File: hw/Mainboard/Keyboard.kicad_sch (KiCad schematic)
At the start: 7 parts, among them J18 KEYBOARD, J19 KEYBOARD_EX, U19 74LS145

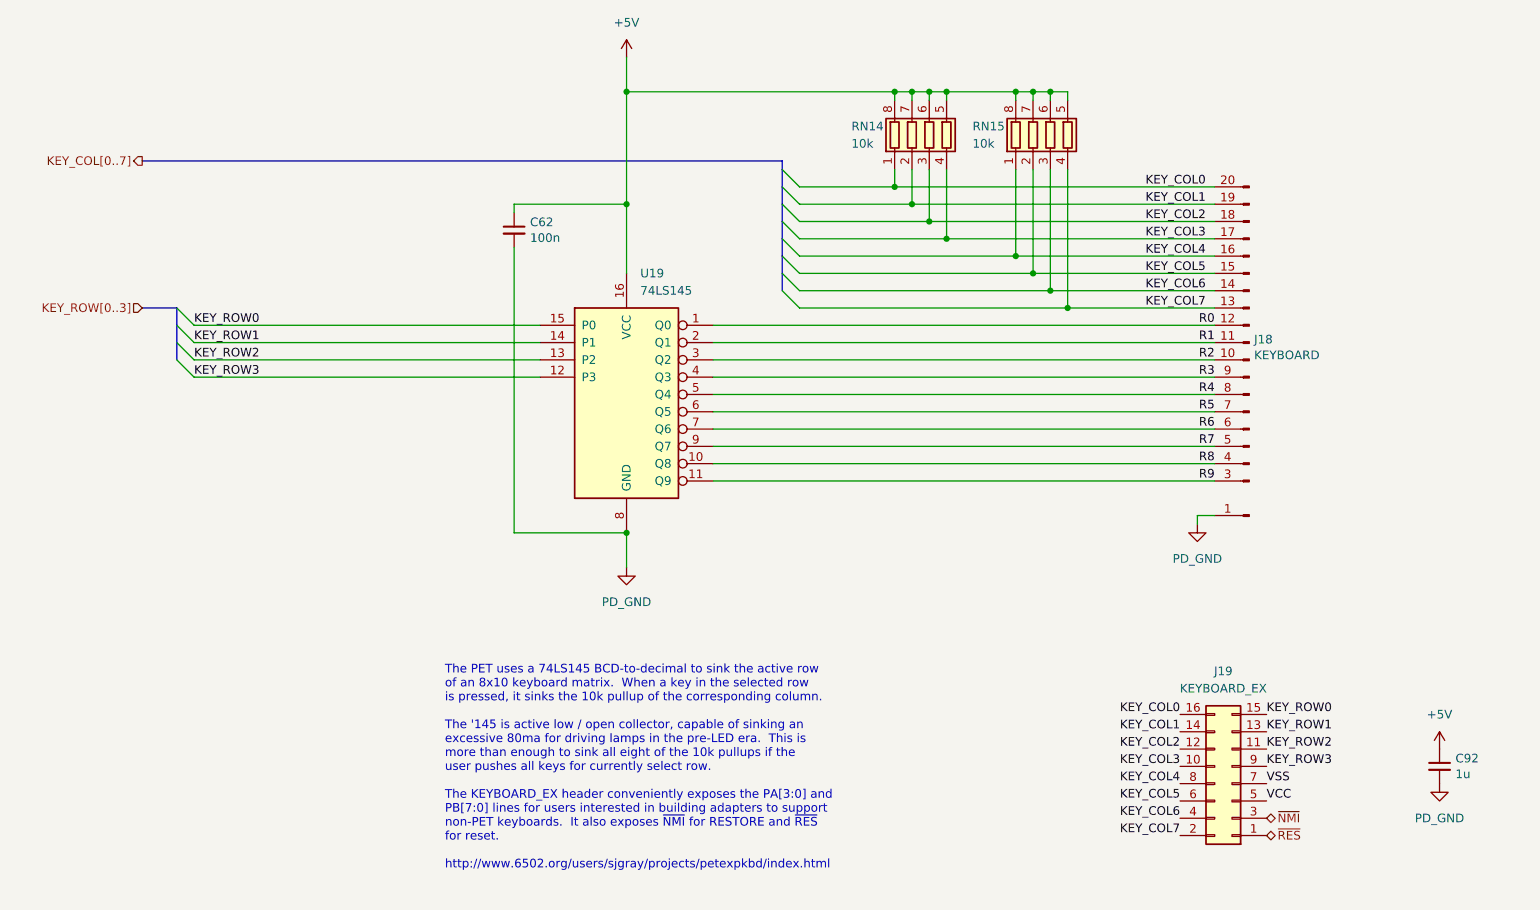
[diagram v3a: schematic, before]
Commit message: hw: renumber J* refs to match PET connectors
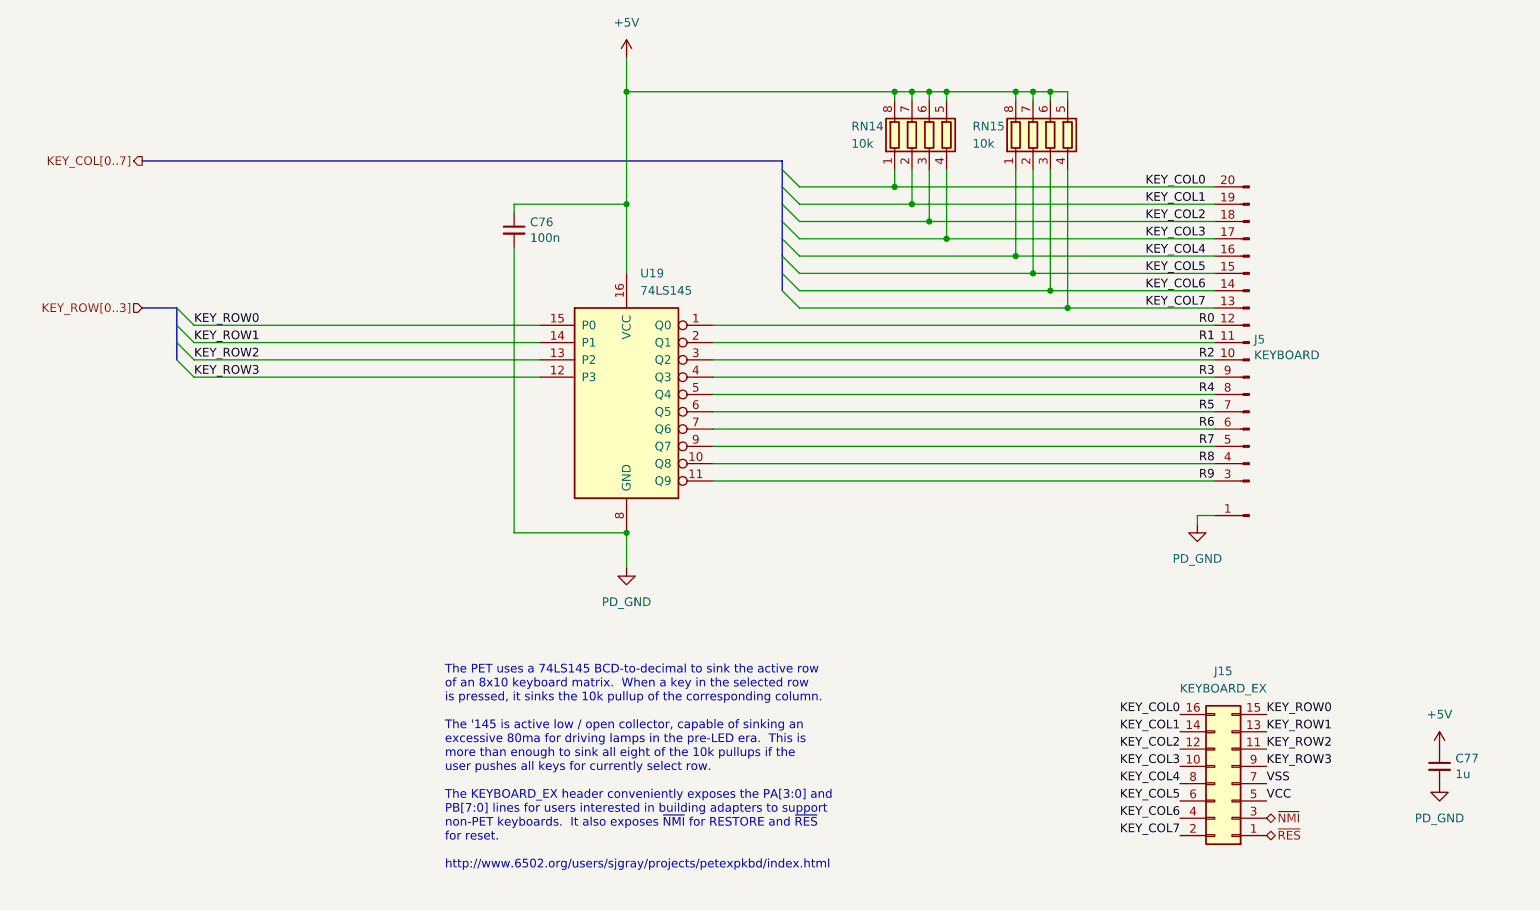
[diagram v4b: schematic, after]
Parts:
- renumbered C62 to C76, C92 to C77, J19 to J15, J18 to J5
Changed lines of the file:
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@@
   (symbol (lib_id "Retrocomputing:CBM_PET_Keyboard_Conn_Keyed_20P") (at 201.93 73.66 180) (unit 1)
     (in_bom yes) (on_board yes)
-    (property "Reference" "J18" (id 0) (at 202.6412 70.6628 0)
+    (property "Reference" "J5" (id 0) (at 202.6412 70.6628 0)
       (effects (font (size 1.27 1.27)) (justify right))
     )
@@
   (symbol (lib_id "Device:C_Small") (at 93.98 54.61 0) (unit 1)
     (in_bom yes) (on_board yes)
-    (property "Reference" "C62" (id 0) (at 96.3168 53.4416 0)
+    (property "Reference" "C76" (id 0) (at 96.3168 53.4416 0)
       (effects (font (size 1.27 1.27)) (justify left))
     )
@@
   (symbol (lib_id "Device:C_Small") (at 229.87 133.35 0) (unit 1)
     (in_bom yes) (on_board yes)
-    (property "Reference" "C92" (id 0) (at 232.2068 132.1816 0)
+    (property "Reference" "C77" (id 0) (at 232.2068 132.1816 0)
       (effects (font (size 1.27 1.27)) (justify left))
     )
@@
   (symbol (lib_id "PET:PD_GND") (at 110.49 104.14 0) (unit 1)
     (in_bom yes) (on_board yes) (fields_autoplaced)
-    (property "Reference" "#PWR0127" (id 0) (at 110.49 110.49 0)
+    (property "Reference" "#PWR0136" (id 0) (at 110.49 110.49 0)
       (effects (font (size 1.27 1.27)) hide)
     )
@@
   (symbol (lib_id "Connector_Generic:Conn_02x08_Odd_Even") (at 199.39 135.89 180) (unit 1)
     (in_bom yes) (on_board yes) (fields_autoplaced)
-    (property "Reference" "J19" (id 0) (at 198.12 119.38 0))
+    (property "Reference" "J15" (id 0) (at 198.12 119.38 0))
     (property "Value" "KEYBOARD_EX" (id 1) (at 198.12 121.92 0))
     (property "Footprint" "Connector_PinHeader_2.54mm:PinHeader_2x08_P2.54mm_Vertical" (id 2) (at 199.39 135.89 0)
@@
   (symbol (lib_id "power:+5V") (at 229.87 130.81 0) (unit 1)
     (in_bom yes) (on_board yes) (fields_autoplaced)
-    (property "Reference" "#PWR0183" (id 0) (at 229.87 134.62 0)
+    (property "Reference" "#PWR0138" (id 0) (at 229.87 134.62 0)
       (effects (font (size 1.27 1.27)) hide)
     )
@@
   (symbol (lib_id "PET:PD_GND") (at 194.31 97.79 0) (unit 1)
     (in_bom yes) (on_board yes) (fields_autoplaced)
-    (property "Reference" "#PWR0126" (id 0) (at 194.31 104.14 0)
+    (property "Reference" "#PWR0137" (id 0) (at 194.31 104.14 0)
       (effects (font (size 1.27 1.27)) hide)
     )
@@
   (symbol (lib_id "power:+5V") (at 110.49 29.21 0) (unit 1)
     (in_bom yes) (on_board yes) (fields_autoplaced)
-    (property "Reference" "#PWR0125" (id 0) (at 110.49 33.02 0)
+    (property "Reference" "#PWR0135" (id 0) (at 110.49 33.02 0)
       (effects (font (size 1.27 1.27)) hide)
     )
@@
   (symbol (lib_id "PET:PD_GND") (at 229.87 135.89 0) (unit 1)
     (in_bom yes) (on_board yes) (fields_autoplaced)
-    (property "Reference" "#PWR0184" (id 0) (at 229.87 142.24 0)
-      (effects (font (size 1.27 1.27)) hide)
-    )
+    (property "Reference" "#PWR0139" (id 0) (at 229.87 142.24 0)
+      (effects (font (size 1.27 1.27)) hide)
+    )

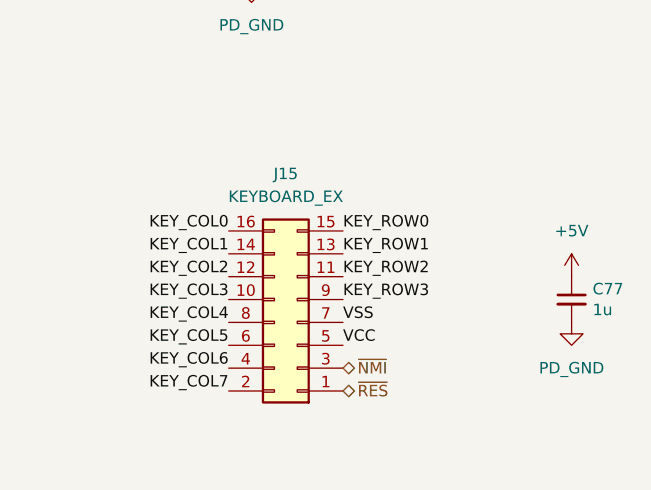
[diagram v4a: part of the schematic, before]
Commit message: hw: renumber rn.  tidy fpga schematics
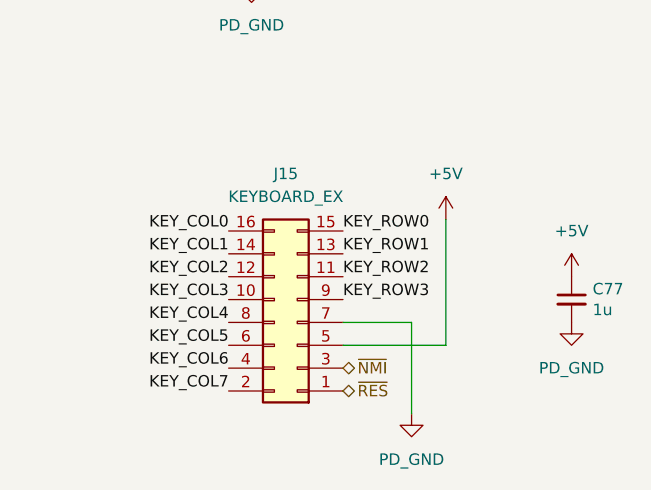
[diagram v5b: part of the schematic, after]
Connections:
- net VCC is gone; now on net +5V: J15.5 (Pin_5)
- net VSS is gone; now on net PD_GND: J15.7 (Pin_7)
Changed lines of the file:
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@@
+    (stroke (width 0) (type default) (color 0 0 0 0))
+  )
+  (wire (pts (xy 204.47 135.89) (xy 212.09 135.89))
     (stroke (width 0) (type default) (color 0 0 0 0))
   )
@@
     (stroke (width 0) (type default) (color 0 0 0 0))
   )
+  (wire (pts (xy 215.9 124.46) (xy 215.9 138.43))
+    (stroke (width 0) (type default) (color 0 0 0 0))
+  )
   (wire (pts (xy 170.18 60.96) (xy 196.85 60.96))
     (stroke (width 0) (type default) (color 0 0 0 0))
@@
     (stroke (width 0) (type default) (color 0 0 0 0))
   )
+  (wire (pts (xy 212.09 135.89) (xy 212.09 146.05))
+    (stroke (width 0) (type default) (color 0 0 0 0))
+  )
   (wire (pts (xy 170.18 34.29) (xy 172.72 34.29))
     (stroke (width 0) (type default) (color 0 0 0 0))
@@
   )
   (wire (pts (xy 123.19 73.66) (xy 196.85 73.66))
+    (stroke (width 0) (type default) (color 0 0 0 0))
+  )
+  (wire (pts (xy 204.47 138.43) (xy 215.9 138.43))
     (stroke (width 0) (type default) (color 0 0 0 0))
   )
@@
     (effects (font (size 1.27 1.27)) (justify left bottom))
   )
-  (label "VSS" (at 204.47 135.89 0)
-    (effects (font (size 1.27 1.27)) (justify left bottom))
-  )
   (label "R9" (at 196.85 91.44 180)
     (effects (font (size 1.27 1.27)) (justify right bottom))
@@
   )
   (label "KEY_COL0" (at 186.69 48.26 0)
-    (effects (font (size 1.27 1.27)) (justify left bottom))
-  )
-  (label "VCC" (at 204.47 138.43 0)
     (effects (font (size 1.27 1.27)) (justify left bottom))
   )
@@
     (pin "2")
   )
+  (symbol (lib_id "power:+5V") (at 215.9 124.46 0) (unit 1)
+    (in_bom yes) (on_board yes) (fields_autoplaced)
+    (property "Reference" "#PWR0180" (id 0) (at 215.9 128.27 0)
+      (effects (font (size 1.27 1.27)) hide)
+    )
+    (property "Value" "+5V" (id 1) (at 215.9 119.38 0))
+    (property "Footprint" "" (id 2) (at 215.9 124.46 0)
+      (effects (font (size 1.27 1.27)) hide)
+    )
+    (property "Datasheet" "" (id 3) (at 215.9 124.46 0)
+      (effects (font (size 1.27 1.27)) hide)
+    )
+    (pin "1")
+  )
   (symbol (lib_id "Device:C_Small") (at 229.87 133.35 0) (unit 1)
     (in_bom yes) (on_board yes)
@@
       (effects (font (size 1.27 1.27)) hide)
     )
+    (pin "1")
+  )
+  (symbol (lib_id "PET:PD_GND") (at 212.09 146.05 0) (unit 1)
+    (in_bom yes) (on_board yes) (fields_autoplaced)
+    (property "Reference" "#PWR0179" (id 0) (at 212.09 152.4 0)
+      (effects (font (size 1.27 1.27)) hide)
+    )
+    (property "Value" "PD_GND" (id 1) (at 212.09 151.13 0))
+    (property "Footprint" "" (id 2) (at 212.09 146.05 0)
+      (effects (font (size 1.27 1.27)) hide)
+    )
+    (property "Datasheet" "" (id 3) (at 212.09 146.05 0)
+      (effects (font (size 1.27 1.27)) hide)
+    )

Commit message: hw: tidy
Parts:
- C77: value 1u -> 4.7u 10V; LCSC C52923 -> C23733
- J5: MPN 2-826646-0 -> (none)
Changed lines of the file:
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@@
-      (effects (font (size 1.27 1.27)) hide)
-    )
-    (property "MPN" "2-826646-0" (id 5) (at 201.93 73.66 0)
       (effects (font (size 1.27 1.27)) hide)
     )
@@
     )
     (pin "1")
-  )
-  (symbol (lib_id "Device:C_Small") (at 229.87 133.35 0) (unit 1)
-    (in_bom yes) (on_board yes)
-    (property "Reference" "C77" (id 0) (at 232.2068 132.1816 0)
-      (effects (font (size 1.27 1.27)) (justify left))
-    )
-    (property "Value" "1u" (id 1) (at 232.2068 134.493 0)
-      (effects (font (size 1.27 1.27)) (justify left))
-    )
-    (property "Footprint" "Capacitor_SMD:C_0402_1005Metric" (id 2) (at 229.87 133.35 0)
-      (effects (font (size 1.27 1.27)) hide)
-    )
-    (property "Datasheet" "https://datasheet.lcsc.com/lcsc/2304140030_Samsung-Electro-Mechanics-CL05A105KA5NQNC_C52923.pdf" (id 3) (at 229.87 133.35 0)
-      (effects (font (size 1.27 1.27)) hide)
-    )
-    (property "LCSC" "C52923" (id 4) (at 229.87 133.35 0)
-      (effects (font (size 1.27 1.27)) hide)
-    )
-    (pin "1")
-    (pin "2")
   )
   (symbol (lib_id "PET:PD_GND") (at 110.49 104.14 0) (unit 1)
@@
     (pin "1")
   )
+  (symbol (lib_id "Device:C_Small") (at 229.87 133.35 0) (unit 1)
+    (in_bom yes) (on_board yes)
+    (property "Reference" "C77" (id 0) (at 232.2068 132.1816 0)
+      (effects (font (size 1.27 1.27)) (justify left))
+    )
+    (property "Value" "4.7u 10V" (id 1) (at 232.2068 134.493 0)
+      (effects (font (size 1.27 1.27)) (justify left))
+    )
+    (property "Footprint" "Capacitor_SMD:C_0402_1005Metric" (id 2) (at 229.87 133.35 0)
+      (effects (font (size 1.27 1.27)) hide)
+    )
+    (property "Datasheet" "https://datasheet.lcsc.com/lcsc/2304140030_Samsung-Electro-Mechanics-CL05A475MP5NRNC_C23733.pdf" (id 3) (at 229.87 133.35 0)
+      (effects (font (size 1.27 1.27)) hide)
+    )
+    (property "LCSC" "C23733" (id 4) (at 229.87 133.35 0)
+      (effects (font (size 1.27 1.27)) hide)
+    )
+    (pin "1")
+    (pin "2")
+  )
   (symbol (lib_id "PET:PD_GND") (at 212.09 146.05 0) (unit 1)
